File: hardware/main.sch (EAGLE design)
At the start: 35 parts, among them IC1 LM358D, T2 BC848ALT1SMD, T3 IRF840, T6 BC848ALT1SMD, T7 BC848ALT1SMD

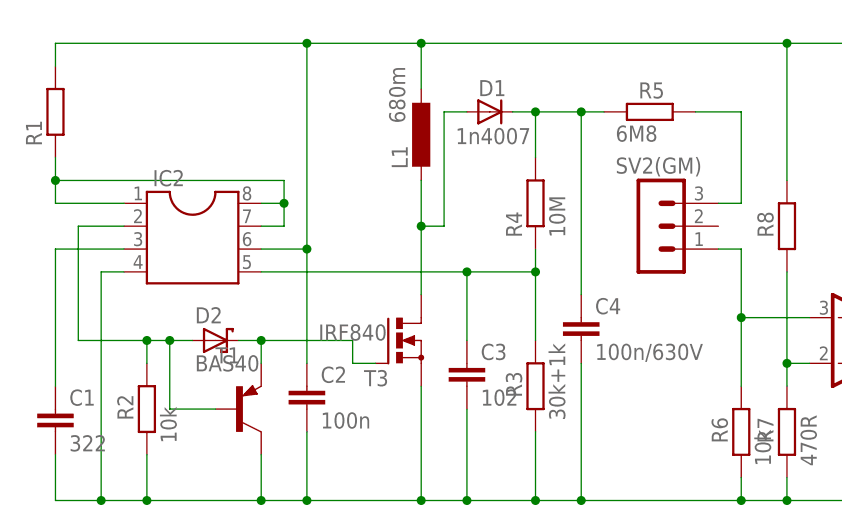
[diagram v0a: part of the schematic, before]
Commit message: Folder structure changed.
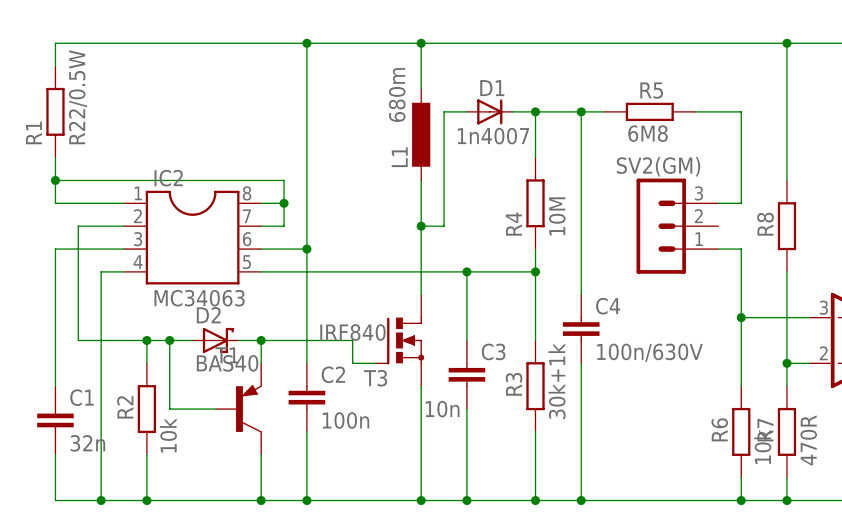
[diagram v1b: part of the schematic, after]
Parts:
- C1: value 322 -> 32n
- C3: value 102 -> 10n
- IC2: value (none) -> MC34063
- R1: value (none) -> R22/0.5W
- R2, R8: device resistor:R-EU_0207/5V -> resistor:R-EU_R1206
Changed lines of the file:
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@@
 <setting verticaltext="up"/>
 </settings>
-<grid distance="0.05" unitdist="inch" unit="inch" style="lines" multiple="1" display="yes" altdistance="0.01" altunitdist="inch" altunit="inch"/>
+<grid distance="0.1" unitdist="inch" unit="inch" style="lines" multiple="1" display="no" altdistance="0.01" altunitdist="inch" altunit="inch"/>
 <layers>
-<layer number="1" name="Top" color="4" fill="1" visible="no" active="no"/>
-<layer number="16" name="Bottom" color="1" fill="1" visible="no" active="no"/>
-<layer number="17" name="Pads" color="2" fill="1" visible="no" active="no"/>
-<layer number="18" name="Vias" color="2" fill="1" visible="no" active="no"/>
-<layer number="19" name="Unrouted" color="6" fill="1" visible="no" active="no"/>
-<layer number="20" name="Dimension" color="15" fill="1" visible="no" active="no"/>
-<layer number="21" name="tPlace" color="7" fill="1" visible="no" active="no"/>
-<layer number="22" name="bPlace" color="7" fill="1" visible="no" active="no"/>
-<layer number="23" name="tOrigins" color="15" fill="1" visible="no" active="no"/>
-<layer number="24" name="bOrigins" color="15" fill="1" visible="no" active="no"/>
-<layer number="25" name="tNames" color="7" fill="1" visible="no" active="no"/>
-<layer number="26" name="bNames" color="7" fill="1" visible="no" active="no"/>
-<layer number="27" name="tValues" color="7" fill="1" visible="no" active="no"/>
-<layer number="28" name="bValues" color="7" fill="1" visible="no" active="no"/>
+<layer number="1" name="Top" color="4" fill="1" visible="yes" active="no"/>
+<layer number="16" name="Bottom" color="1" fill="1" visible="yes" active="no"/>
+<layer number="17" name="Pads" color="2" fill="1" visible="yes" active="no"/>
+<layer number="18" name="Vias" color="2" fill="1" visible="yes" active="no"/>
+<layer number="19" name="Unrouted" color="6" fill="1" visible="yes" active="no"/>
+<layer number="20" name="Dimension" color="15" fill="1" visible="yes" active="no"/>
+<layer number="21" name="tPlace" color="7" fill="1" visible="yes" active="no"/>
+<layer number="22" name="bPlace" color="7" fill="1" visible="yes" active="no"/>
+<layer number="23" name="tOrigins" color="15" fill="1" visible="yes" active="no"/>
+<layer number="24" name="bOrigins" color="15" fill="1" visible="yes" active="no"/>
+<layer number="25" name="tNames" color="7" fill="1" visible="yes" active="no"/>
+<layer number="26" name="bNames" color="7" fill="1" visible="yes" active="no"/>
+<layer number="27" name="tValues" color="7" fill="1" visible="yes" active="no"/>
+<layer number="28" name="bValues" color="7" fill="1" visible="yes" active="no"/>
 <layer number="29" name="tStop" color="7" fill="3" visible="no" active="no"/>
 <layer number="30" name="bStop" color="7" fill="6" visible="no" active="no"/>
@@
 <layer number="35" name="tGlue" color="7" fill="4" visible="no" active="no"/>
 <layer number="36" name="bGlue" color="7" fill="5" visible="no" active="no"/>
-<layer number="37" name="tTest" color="7" fill="1" visible="no" active="no"/>
-<layer number="38" name="bTest" color="7" fill="1" visible="no" active="no"/>
+<layer number="37" name="tTest" color="7" fill="1" visible="yes" active="no"/>
+<layer number="38" name="bTest" color="7" fill="1" visible="yes" active="no"/>
 <layer number="39" name="tKeepout" color="4" fill="11" visible="no" active="no"/>
 <layer number="40" name="bKeepout" color="1" fill="11" visible="no" active="no"/>
@@
 <layer number="44" name="Drills" color="7" fill="1" visible="no" active="no"/>
 <layer number="45" name="Holes" color="7" fill="1" visible="no" active="no"/>
-<layer number="46" name="Milling" color="3" fill="1" visible="no" active="no"/>
-<layer number="47" name="Measures" color="7" fill="1" visible="no" active="no"/>
-<layer number="48" name="Document" color="7" fill="1" visible="no" active="no"/>
-<layer number="49" name="Reference" color="7" fill="1" visible="no" active="no"/>
-<layer number="51" name="tDocu" color="7" fill="1" visible="no" active="no"/>
-<layer number="52" name="bDocu" color="7" fill="1" visible="no" active="no"/>
+<layer number="46" name="Milling" color="3" fill="1" visible="yes" active="no"/>
+<layer number="47" name="Measures" color="7" fill="1" visible="yes" active="no"/>
+<layer number="48" name="Document" color="7" fill="1" visible="yes" active="no"/>
+<layer number="49" name="Reference" color="7" fill="1" visible="yes" active="no"/>
+<layer number="51" name="tDocu" color="7" fill="1" visible="yes" active="no"/>
+<layer number="52" name="bDocu" color="7" fill="1" visible="yes" active="no"/>
 <layer number="90" name="Modules" color="5" fill="1" visible="yes" active="yes"/>
 <layer number="91" name="Nets" color="2" fill="1" visible="yes" active="yes"/>
@@
 <part name="IC1" library="linear" deviceset="LM358" device="D" value="LM358D"/>
 <part name="R7" library="resistor" deviceset="R-EU_" device="0207/5V" value="470R"/>
-<part name="R8" library="resistor" deviceset="R-EU_" device="0207/5V"/>
+<part name="R8" library="resistor" deviceset="R-EU_" device="R1206"/>
 <part name="SV3(OUT)" library="con-lstb" deviceset="MA03-1" device=""/>
 <part name="SV2(GM)" library="con-lstb" deviceset="MA03-1" device=""/>
 <part name="SV4(POWER)" library="con-lstb" deviceset="MA03-1" device=""/>
-<part name="C3" library="resistor" deviceset="C-EU" device="050-025X075" value="102"/>
+<part name="C3" library="resistor" deviceset="C-EU" device="050-025X075" value="10n"/>
 <part name="R5" library="resistor" deviceset="R-EU_" device="0207/12" value="6M8"/>
 <part name="C5" library="resistor" deviceset="C-EU" device="C3216" value="100n"/>
 <part name="L1" library="resistor" deviceset="L-EU" device="0207/5V" value="680m"/>
 <part name="C4" library="resistor" deviceset="C-EU" device="102-064X133" value="100n/630V"/>
-<part name="R2" library="resistor" deviceset="R-EU_" device="0207/5V" value="10k"/>
+<part name="R2" library="resistor" deviceset="R-EU_" device="R1206" value="10k"/>
 <part name="D2" library="diode" deviceset="BAS40" device=""/>
 <part name="T2" library="transistor-npn" deviceset="BC848*" device="SMD" technology="ALT1" value=""/>
-<part name="IC2" library="ic-package" deviceset="DIL8" device=""/>
-<part name="C1" library="resistor" deviceset="C-EU" device="050-025X075" value="322"/>
-<part name="R1" library="resistor" deviceset="R-EU_" device="0207/5V"/>
+<part name="IC2" library="ic-package" deviceset="DIL8" device="" value="MC34063"/>
+<part name="C1" library="resistor" deviceset="C-EU" device="050-025X075" value="32n"/>
+<part name="R1" library="resistor" deviceset="R-EU_" device="0207/5V" value="R22/0.5W"/>
 <part name="C2" library="resistor" deviceset="C-EU" device="C3216" value="100n"/>
 <part name="C7" library="resistor" deviceset="CPOL-US" device="A/3216-18W" value="330u"/>
@@
 <attribute name="NAME" x="118.11" y="59.182" size="1.778" layer="95" rot="MR0"/>
 </instance>
-<instance part="C3" gate="G$1" x="-45.72" y="40.64"/>
+<instance part="C3" gate="G$1" x="-45.72" y="40.64" smashed="yes">
+<attribute name="NAME" x="-44.196" y="41.021" size="1.778" layer="95"/>
+<attribute name="VALUE" x="-50.546" y="34.671" size="1.778" layer="96"/>
+</instance>
 <instance part="IC1" gate="P" x="81.28" y="50.8"/>
 <instance part="R5" gate="G$1" x="-25.4" y="68.58" smashed="yes">
 <attribute name="NAME" x="-26.67" y="70.0786" size="1.778" layer="95"/>
-<attribute name="VALUE" x="-29.21" y="65.278" size="1.778" layer="96"/>
+<attribute name="VALUE" x="-27.94" y="65.278" size="1.778" layer="96"/>
 </instance>
 <instance part="C5" gate="G$1" x="73.66" y="50.8"/>
@@
 <instance part="R2" gate="G$1" x="-81.28" y="35.56" smashed="yes" rot="R90">
 <attribute name="NAME" x="-82.7786" y="34.29" size="1.778" layer="95" rot="R90"/>
-<attribute name="VALUE" x="-77.978" y="31.75" size="1.778" layer="96" rot="R90"/>
+<attribute name="VALUE" x="-77.978" y="30.48" size="1.778" layer="96" rot="R90"/>
 </instance>
 <instance part="D2" gate="1" x="-73.66" y="43.18"/>

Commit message: PCB is now fixed.
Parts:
- removed IC1: LM358D, linear:LM358D
- removed SV2(GM), SV3(OUT), SV4(POWER): (no value), con-lstb:MA03-1
- removed T2, T6, T7: BC848ALT1SMD, transistor-npn:BC848ALT1SMD
- removed T3: IRF840, transistor-power:BUZ11BV
- added IC3: MC34063AD, mc34063:MC34063AD
- added J1, J2: 22-05-7028-02, con-molex:22-05-7028-02
- added JP1: (no value), jumper:JP1E
- added Q1: IRF840, transistor-power:BUZ11BV
- added Q2, Q3, Q4: BC848ALT1SMD, transistor-npn:BC848ALT1SMD
- added R14: (no value), resistor:R-EU_M0805
- added SV2: (no value), con-lstb:MA03-1
- C1: device resistor:C-EU050-025X075 -> resistor:C-EUC0805
- C2: value 100n -> 32n; device resistor:C-EUC3216 -> resistor:C-EUC0805
- C3: value 10n -> 100n; device resistor:C-EU050-025X075 -> resistor:C-EUC0805
- C4: value 100n/630V -> 10n; device resistor:C-EU102-064X133 -> resistor:C-EUC0805
- C5: value 100n -> 100n/630V; device resistor:C-EUC3216 -> resistor:C-EU102-064X133
- C6: value 330u -> 100n; device resistor:CPOL-USA/3216-18W -> resistor:C-EUC0805
- C7: device resistor:CPOL-USA/3216-18W -> rcl:CPOL-EUD/7343-31R
- D1: value 1n4007 -> BAS40; device diode:1N4004 -> diode:BAS40
- D2: value BAS40 -> 1n4007; device diode:BAS40 -> diode:1N4004
- IC2: value MC34063 -> LM358D; device ic-package:DIL8 -> linear:LM358D
- R1: value R22/0.5W -> 10k; device resistor:R-EU_0207/5V -> resistor:R-EU_R0805
- R10, R11: device resistor:R-EU_M1206 -> resistor:R-EU_M0805
- R12: value 510R -> 1k; device resistor:R-EU_M1206 -> resistor:R-EU_M0805
- R13: value (none) -> 510R; device resistor:R-EU_M1206 -> resistor:R-EU_M0805
- R2: value 10k -> R22/0.5W; device resistor:R-EU_R1206 -> resistor:R-EU_0207/5V
- R3: value 30k+1k -> 10M
- R4: value 10M -> 30k+1k; device resistor:R-EU_0207/5V -> resistor:R-EU_R0805
- R5: value 6M8 -> 30k+1k; device resistor:R-EU_0207/12 -> resistor:R-EU_R0805
- R6: value 10k -> 6M8
- R7: value 470R -> 10k
- R8: device resistor:R-EU_R1206 -> resistor:R-EU_R0805
- R9: value 1k -> 470R; device resistor:R-EU_M1206 -> resistor:R-EU_R0805
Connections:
- removed net N$20: R5.2, SV2(GM).3
- new net N$18: J2-1.S, R6.2
- new net N$7: IC3.DC, IC3.IS, IC3.SWC, L1.1, R2.1
- net N$1: now also Q4.B, R12.2; no longer R9.2, T7.B
- net N$10: now also Q2.B, R10.2; no longer R11.2, T2.B
- net N$11: now also R4.1, R5.2; no longer IC2.1, IC2.7, IC2.8, R1.1
- net N$12: now also C5.1, D2.C, R3.2, R6.1; no longer C4.1, D1.C, R4.2, R5.1
- net N$13: now also C4.1, IC3.FB, R3.1, R4.2; no longer C3.1, IC2.5, R3.2, R4.1
- net N$14: now also D1.A, IC3.SWE, R1.2; no longer D2.A, IC2.2, R2.2
- net N$15: now also D2.A, Q1.D; no longer D1.A, T3.D
- net N$16: now also D1.C, Q1.G; no longer D2.C, T3.G
- net N$17: now also IC2A.+IN, J2-2.S, R7.2; no longer IC1A.+IN, R6.2, SV2(GM).1
- net N$19: now also IC2A.-IN, R9.2; no longer IC1A.-IN, R7.2
- net N$2: now also Q3.B, R11.2; no longer R10.2, T6.B
- net N$21: now also JP1.2, R14.2, SV2.3; no longer R13.2, SV3(OUT).3
- net N$22: now also IC2B.-IN, IC2B.OUT; no longer IC1B.-IN, IC1B.OUT
- net N$3: now also Q3.C; no longer T6.C
- net N$4: now also Q4.C, R14.1, SV2.2; no longer R13.1, SV3(OUT).2, T7.C
- net N$5: now also C2.1, IC3.TC; no longer IC2.3
- net N$6: now also R13.1; no longer R12.1
- net N$8: now also IC2A.OUT, R12.1; no longer IC1A.OUT, R9.1
- net N$9: now also Q2.C; no longer T2.C
- net V+: now also C3.1, C6.1, IC2P.V+, IC3.VCC, J1-1.S, JP1.1, R13.2, R2.2; no longer C2.1, C5.1, C6.+, IC1P.V+, IC2.6, L1.1, R1.2, R12.2, SV4(POWER).3
- net V-: now also C6.2, IC2B.+IN, IC2P.V-, IC3.GND, J1-2.S, Q1.S, Q2.E, Q3.E, Q4.E, R1.1, R5.1, R9.1, SV2.1; no longer C6.-, IC1B.+IN, IC1P.V-, IC2.4, R2.1, R3.1, R6.1, SV3(OUT).1, SV4(POWER).1, T2.E, T3.S, T6.E, T7.E
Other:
- note added: "5V/400V DC/DC converter"
- note added: "GM detector"
- note added: "Output"
- note added: "Power supply"
- moved on the sheet: C1, C2, C3, C4, C5, C7, L1, LED1, R1, R10, R11, R12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
